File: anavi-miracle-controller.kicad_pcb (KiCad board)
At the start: 2 copper layers, 74.9 x 40.6 mm, 31 parts, among them P1 CONN_01X03, U1 I2C_SENS_1, U2 I2C_SENS_1, U3 I2C_SENS_1

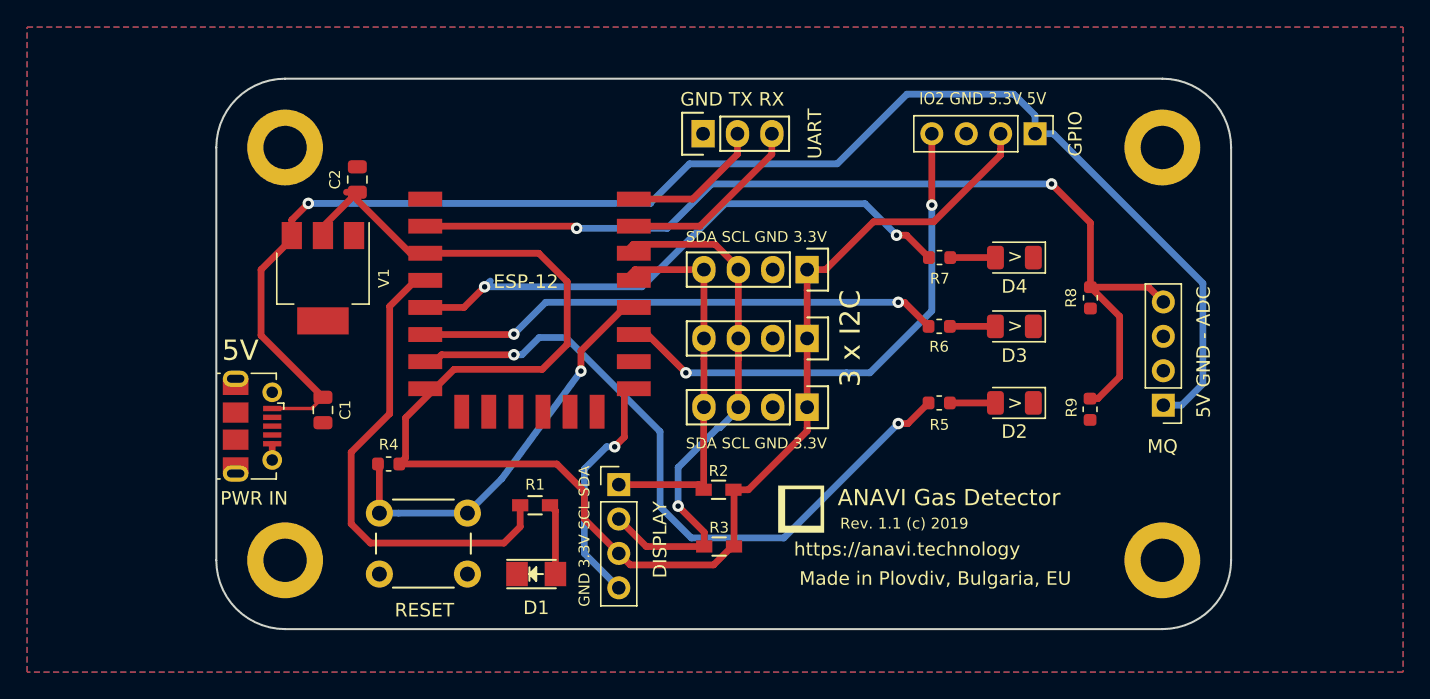
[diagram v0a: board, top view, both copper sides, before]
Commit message: Update schematics and PCB design
Major update to add SN74AHCT125D and to make the PCB design.

Signed-off-by: Leon Anavi <leon@anavi.org>
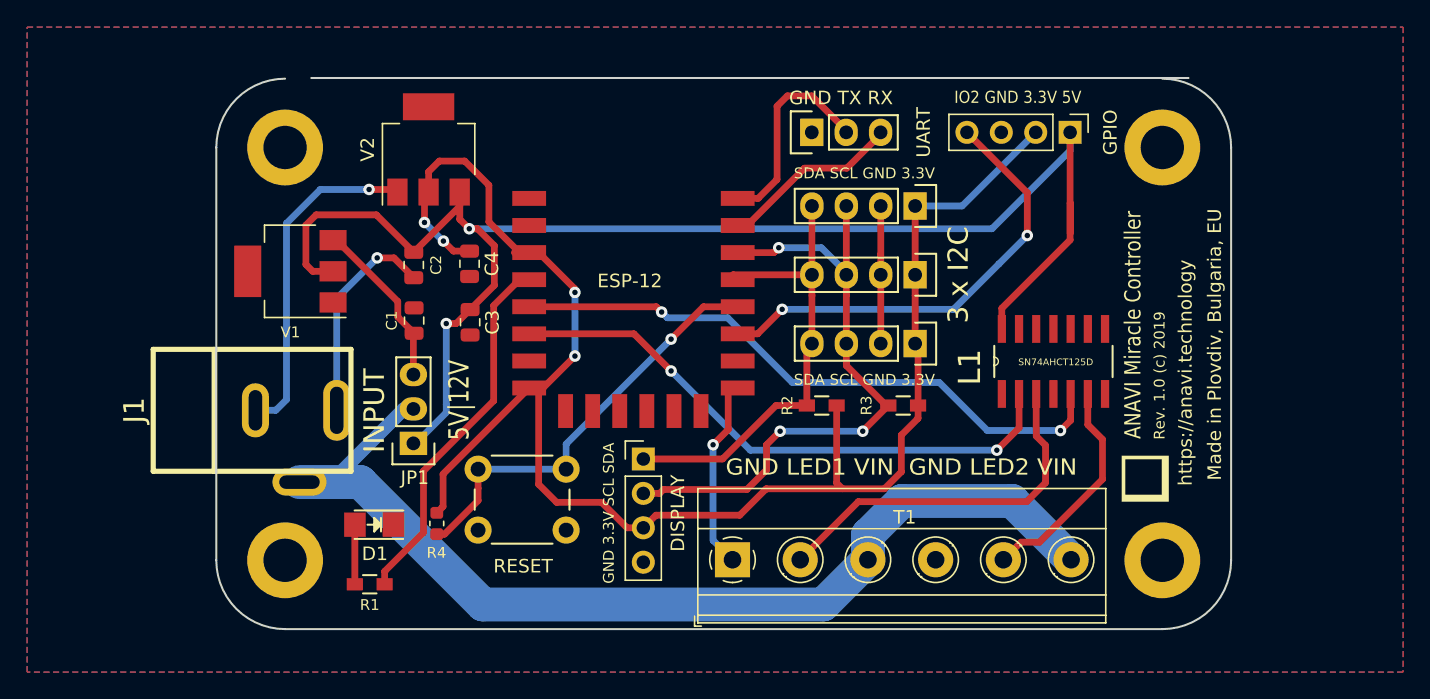
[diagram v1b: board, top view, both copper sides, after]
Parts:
- removed D2: KP-3216SGC, LED_SMD:LED_1206_3216Metric
- removed D3: KP-3216YC, LED_SMD:LED_1206_3216Metric
- removed D4: KP-3216EC, LED_SMD:LED_1206_3216Metric
- removed MQ: Conn_01x04, Connector_PinHeader_2.54mm:PinHeader_1x04_P2.54mm_Vertical
- removed PWR IN: USB_B_Micro, Connector_USB:USB_Micro-B_Molex-105017-0001
- removed R5, R6, R7: 68R, Resistor_SMD:R_0603_1608Metric
- removed R8: 220K, Resistor_SMD:R_0603_1608Metric
- removed R9: 56K, Resistor_SMD:R_0603_1608Metric
- added C3: 10uF, Capacitor_SMD:C_0805_2012Metric, F.Cu at (83.5, 89.1)
- added C4: 10uF, Capacitor_SMD:C_0805_2012Metric, F.Cu at (83.5, 84.8)
- added J1: INPUT, w_conn_misc:dc_socket, F.Cu at (67.4, 95.6)
- added JP1: SolderJumper_3_Open, Pin_Headers:Pin_Header_Straight_1x03, F.Cu at (79.3, 98.0)
- added L1: SN74AHCT125D, SOIC127P600X175-14N, F.Cu at (130.4, 89.6)
- added T1: Screw_Terminal_01x06, TerminalBlock_Phoenix:TerminalBlock_Phoenix_MKDS-1,5-6_1x06_P5.00mm_Horizontal, F.Cu at (102.9, 106.6)
- added V2: LD1117S33TR, Package_TO_SOT_SMD:SOT-223, F.Cu at (80.4, 76.3)
- V1: value LD1117S33TR -> NCP1117ST50T3G
- moved G*** 25.6 mm to (133.4, 100.7), turned to 90 degrees
- moved R3 17.1 mm to (115.5, 95.2)
- moved R1 13.5 mm to (76.1, 108.5), turned to 180 degrees
- moved D1 12.5 mm to (76.4, 104.0), turned to 180 degrees
- moved R2 9.84 mm to (109.5, 95.2)
- moved C1 9.43 mm to (79.4, 89.0), turned to 90 degrees
- moved U1 9.26 mm to (116.4, 90.7)
- moved U2 9.26 mm to (116.4, 85.6)
- moved U3 9.26 mm to (116.4, 80.5)
- moved P1 8.03 mm to (108.7, 75.1)
- moved RESET 7.98 mm to (90.6, 104.5)
- moved ESP-12 7.67 mm to (88.6, 80.0)
- moved C2 7.56 mm to (79.3, 84.9), turned to 270 degrees
- moved R4 5.65 mm to (81.0, 104.0), turned to 90 degrees
- moved DISPLAY 2.62 mm to (96.3, 99.2)
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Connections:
- C1 pad 1: +5V -> +12V
- C2 pad 1: +3V3 -> +5V
- ESP-12 pad 1: Net-(ESP-12-Pad1) -> (no net)
- ESP-12 pad 17: Net-(ESP-12-Pad17) -> (no net)
- ESP-12 pad 18: Net-(ESP-12-Pad18) -> (no net)
- ESP-12 pad 19: Net-(ESP-12-Pad19) -> (no net)
- ESP-12 pad 2: Net-(ESP-12-Pad2) -> (no net)
- ESP-12 pad 20: Net-(ESP-12-Pad20) -> (no net)
- ESP-12 pad 21: Net-(ESP-12-Pad21) -> (no net)
- ESP-12 pad 22: Net-(ESP-12-Pad22) -> (no net)
- ESP-12 pad 7: Net-(ESP-12-Pad7) -> (no net)
- V1 pad 2: +3V3 -> +5V
- V1 pad 3: +5V -> +12V
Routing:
- net Net-(J1-Pad1): track 0.00 -> 77.6 mm
- net Net-(ESP-12-Pad2): track 72.0 -> 0.00 mm, vias 2 -> 0
- net Net-(ESP-12-Pad7): track 50.7 -> 0.00 mm, vias 2 -> 0
- net GND: track 18.5 -> 65.9 mm, vias 1 -> 3
- net /LED1: track 0.00 -> 27.3 mm
- net /LED2: track 0.00 -> 16.5 mm
- net +12V: track 0.00 -> 12.6 mm
- net Net-(ESP-12-Pad14): track 39.9 -> 48.2 mm, vias 1 -> 3
- net Net-(ESP-12-Pad4): track 36.5 -> 29.2 mm
- net Net-(ESP-12-Pad13): track 29.9 -> 35.6 mm
- net Net-(ESP-12-Pad16): track 11.2 -> 16.2 mm
- net +3V3: track 118.7 -> 123.0 mm, vias 0 -> 4
- net Net-(ESP-12-Pad6): track 38.2 -> 42.2 mm
- net Net-(ESP-12-Pad5): track 41.9 -> 45.3 mm
- net Net-(D2-Pad2): track 3.36 -> 0.00 mm
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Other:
- board size 74.9 x 40.6 mm -> 74.9 x 40.7 mm
- board text added: "5V|12V"
- board text added: "ANAVI Miracle Controller"
- board text added: "GND LED1 VIN GND LED2 VIN"
- board text added: "Rev. 1.0 (c) 2019"
- board text removed: "5V"
- board text removed: "5V GND - ADC"
- board text removed: ">"
- board text removed: "ANAVI Gas Detector"
- board text removed: "Rev. 1.1 (c) 2019"

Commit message: anavi-miracle-controller.kicad_pcb: Fix outline
Fix the outline to export properly gerber and drill files.

Signed-off-by: Leon Anavi <leon@anavi.org>
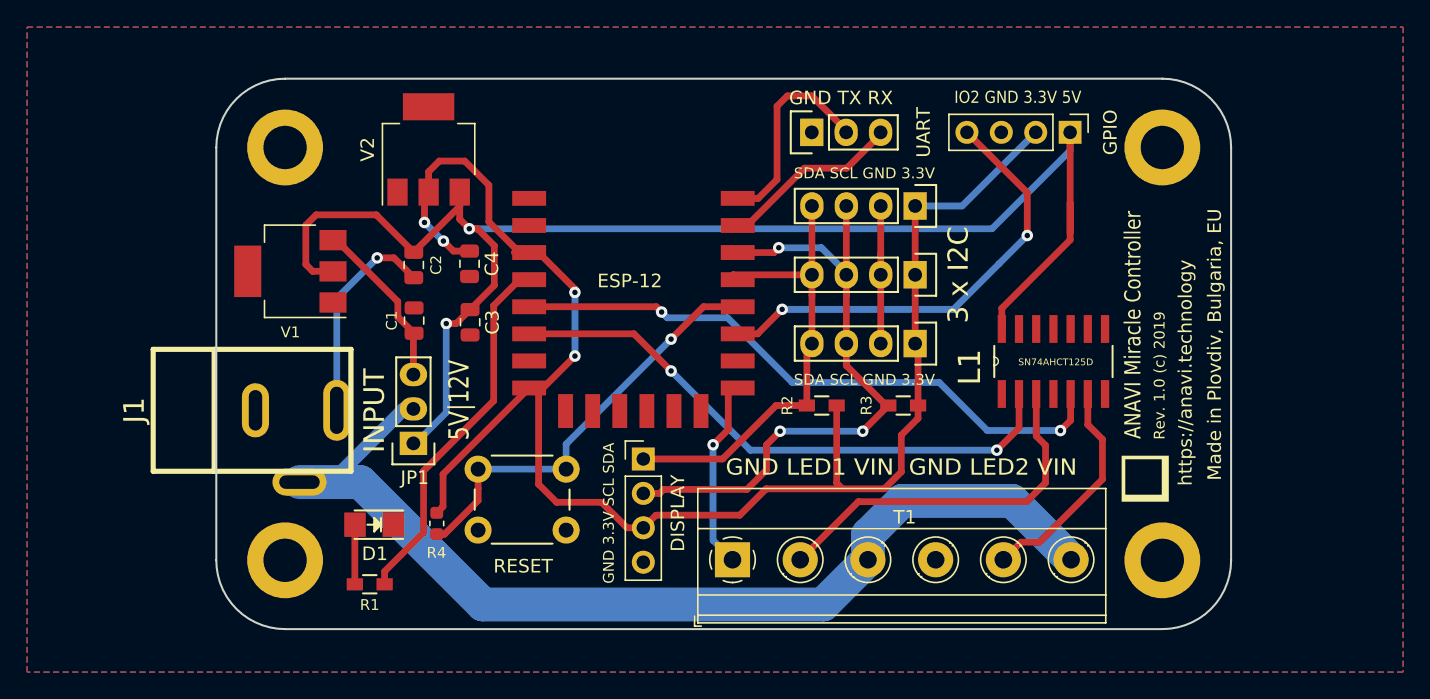
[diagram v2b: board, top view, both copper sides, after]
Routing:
- net GND: track 65.9 -> 41.2 mm, vias 3 -> 2
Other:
- board size 74.9 x 40.7 mm -> 74.9 x 40.6 mm
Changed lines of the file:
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@@
     (thickness 1.6)
     (drawings 22)
-    (tracks 244)
+    (tracks 237)
     (zones 0)
     (modules 28)
@@
       (drillshape 0)
       (scaleselection 1)
-      (outputdirectory "plots/anavi-gas-detector-r1.1/"))
+      (outputdirectory "plots/anavi-miracle-controller-10/"))
   )
   (net 0 "")
@@
     (effects (font (size 1.5 1.5) (thickness 0.25)))
   )
-  (gr_line (start 71.7804 71.0692) (end 136.5504 71.0692) (angle 90) (layer Edge.Cuts) (width 0.15))
+  (gr_line (start 69.85 71.12) (end 134.62 71.12) (angle 90) (layer Edge.Cuts) (width 0.15))
   (gr_line (start 69.85 111.76) (end 134.62 111.76) (angle 90) (layer Edge.Cuts) (width 0.15))
   (gr_arc (start 69.85 76.2) (end 64.77 76.2) (angle 90) (layer Edge.Cuts) (width 0.15))
@@
   (segment (start 101.45 105.20542) (end 102.88394 106.63936) (width 0.5) (layer B.Cu) (net 2))
   (segment (start 101.45 98.15) (end 101.45 105.20542) (width 0.5) (layer B.Cu) (net 2))
-  (via (at 76.05 79.3) (size 0.85) (drill 0.4) (layers F.Cu B.Cu) (net 2))
   (segment (start 77.95464 79.3) (end 78.14688 79.49224) (width 0.5) (layer F.Cu) (net 2))
-  (segment (start 76.05 79.3) (end 77.95464 79.3) (width 0.5) (layer F.Cu) (net 2))
-  (via (at 76.65 84.35) (size 0.85) (drill 0.4) (layers F.Cu B.Cu) (net 2))
   (segment (start 77.88776 84.35) (end 79.3496 85.81184) (width 0.5) (layer F.Cu) (net 2))
   (segment (start 76.65 84.35) (end 77.88776 84.35) (width 0.5) (layer F.Cu) (net 2))
+  (via (at 76.65 84.35) (size 0.85) (drill 0.4) (layers F.Cu B.Cu) (net 2))
   (segment (start 73.66254 87.33746) (end 76.65 84.35) (width 0.5) (layer B.Cu) (net 2))
   (segment (start 73.66254 95.6056) (end 73.66254 87.33746) (width 0.5) (layer B.Cu) (net 2))
-  (segment (start 67.66052 95.6056) (end 69.16001 95.6056) (width 0.5) (layer B.Cu) (net 2))
-  (segment (start 69.16001 95.6056) (end 69.95 94.81561) (width 0.5) (layer B.Cu) (net 2))
-  (segment (start 69.95 81.8) (end 72.45 79.3) (width 0.5) (layer B.Cu) (net 2))
-  (segment (start 72.45 79.3) (end 76.05 79.3) (width 0.5) (layer B.Cu) (net 2))
-  (segment (start 69.95 94.81561) (end 69.95 81.8) (width 0.5) (layer B.Cu) (net 2))
   (segment (start 116.2636 80.4115) (end 116.3701 80.518) (width 0.5) (layer F.Cu) (net 3))
   (segment (start 116.3701 82.034) (end 116.3701 85.598) (width 0.5) (layer F.Cu) (net 3))

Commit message: anavi-miracle-controller.kicad_pcb: Labels
Improve text labels and their positions.

Signed-off-by: Leon Anavi <leon@anavi.org>
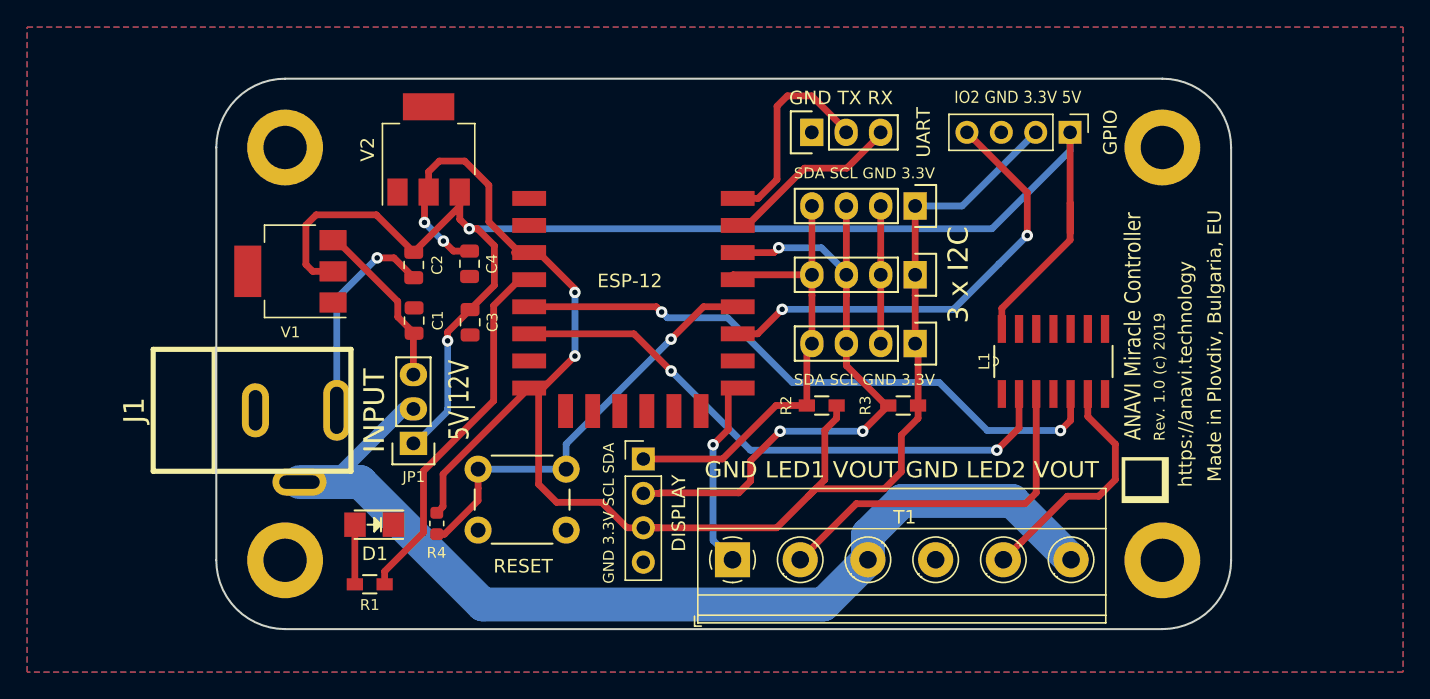
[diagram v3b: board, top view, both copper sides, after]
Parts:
- added ?: , , F.Cu at (116.2, 93.8)
- added ?: , , F.Cu at (116.6, 94.0)
- added ?: , , F.Cu at (116.3, 93.7)
- V2: value LD1117S33TR -> NCP1117ST33T3G
- moved G*** 0.10 mm to (133.4, 100.8)
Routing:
- net +3V3: track 123.0 -> 125.4 mm
- net /LED2: track 16.5 -> 17.9 mm
- net /LED1: track 27.3 -> 26.8 mm
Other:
- board text added: "GND LED1 VOUT GND LED2 VOUT"
- board text added: "SN74AHCT125D"
- board text removed: "GND LED1 VIN GND LED2 VIN"

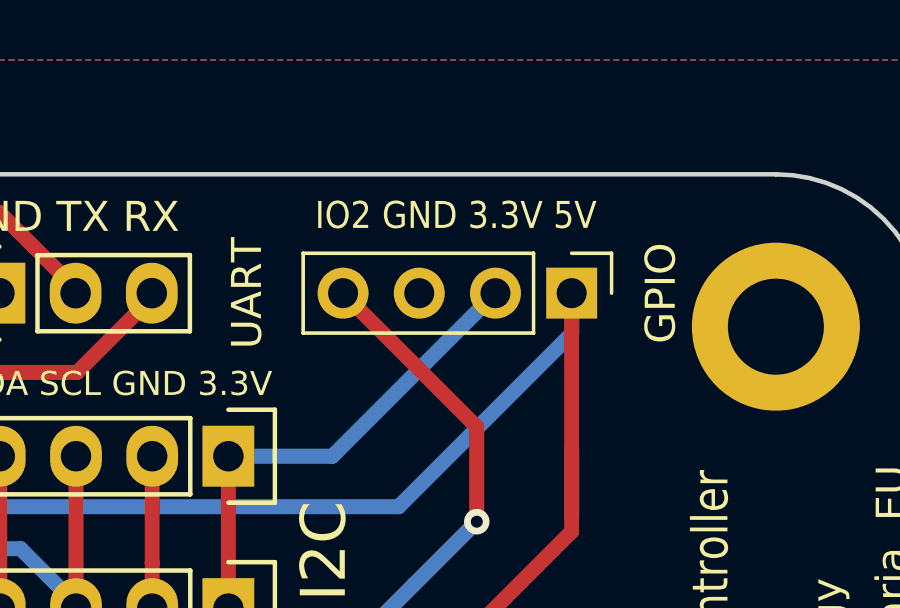
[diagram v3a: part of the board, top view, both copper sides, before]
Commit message: anavi-miracle-controller.kicad_pcb: Improvements
Minor improvements of rev 1.0.

Signed-off-by: Leon Anavi <leon@anavi.org>
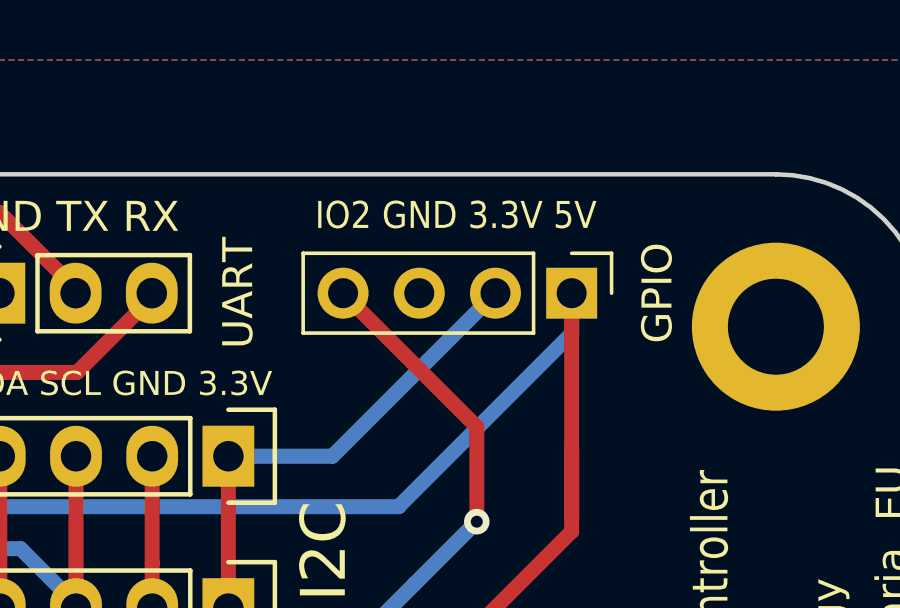
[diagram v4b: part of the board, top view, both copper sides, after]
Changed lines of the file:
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@@
     (descr "Through hole straight pin header, 1x04, 2.54mm pitch, single row")
     (tags "Through hole pin header THT 1x04 2.54mm single row")
-    (fp_text reference GPIO (at 0 -2.9718 270) (layer F.SilkS)
+    (fp_text reference GPIO (at -0.0074 -2.8622 270) (layer F.SilkS)
       (effects (font (size 1 1) (thickness 0.2)))
     )
@@
     (fp_line (start 1.8 9.4) (end 1.8 -1.8) (layer F.CrtYd) (width 0.05))
     (fp_line (start 1.8 -1.8) (end -1.8 -1.8) (layer F.CrtYd) (width 0.05))
-    (fp_text user %R (at 0 3.81) (layer F.Fab)
+    (fp_text user %R (at 0 3.81) (layer F.Fab) hide
       (effects (font (size 1 1) (thickness 0.15)))
     )
@@
     (effects (font (size 1.5 1.2) (thickness 0.25)))
   )
-  (gr_text UART (at 116.9924 75.0824 90) (layer F.SilkS)
+  (gr_text UART (at 116.7 75.075 90) (layer F.SilkS)
     (effects (font (size 1 1) (thickness 0.2)))
   )
